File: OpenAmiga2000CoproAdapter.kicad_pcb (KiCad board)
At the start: 2 copper layers, 188.6 x 114.2 mm, 74 parts, among them CN1 A2000_COPRO_SLOT, P1 CONN_2, P10 CONN_1, P11 CONN_1, P12 CONN_1, P13 CONN_1, P14 CONN_1, P15 CONN_1, P2 CONN_2, P3 CONN_2, P4 CONN_2, P5 CONN_1, P6 CONN_1, P7 CONN_1, P8 CONN_1, P9 CONN_1, P99 OSHW_LOGO, U1 68000D, U10 Spare, U11 74HCT00, U12 74HCT27, U13 74HCT74, U14 74F86, U15 74F74, U16 74HCT04, U17 74HCT112, U18 74F157, U19 74F157, U2 AS6C4008-55PCN, U3 AS6C4008-55PCN, U4 AS6C4008-55PCN, U5 AS6C4008-55PCN, U6 74HCT00, U7 74HCT32, U8 74HCT32, U9 74LS05

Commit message: fix connector
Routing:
- net /~vpa: track 135.8 -> 135.2 mm
- net /e: track 105.2 -> 104.6 mm
- net /r_~w: track 191.0 -> 190.4 mm

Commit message: update silk screen
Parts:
- JP1: value 256K_512K -> 256K 512K
- JP10: value Turbo_SRAM -> Turbo SRAM
- JP2: value 1MB_512K -> 1MB xxxKB
- JP3: value Bank2 -> Bank 2
- JP4: value ROM_R_W -> ROM SW
- JP5: value Bank1_ON_OFF -> Bank 1
- JP6: value Mirror_OFF_ON -> Mirror 256K
- JP7: value Turbo -> Turbo SW
- JP8: value Bank2 D0_C0 -> Bank 2
- JP9: value Turbo_ROM -> Turbo ROM
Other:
- board text added: "C0 D0"
- board text added: "ON OFF"
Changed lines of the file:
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@@
   (general
     (thickness 1.6)
-    (drawings 121)
+    (drawings 124)
     (tracks 2299)
     (zones 0)
@@
     (descr "Through hole straight pin header, 1x03, 2.54mm pitch, single row")
     (tags "Through hole pin header THT 1x03 2.54mm single row")
-    (fp_text reference JP7 (at 0 -2.33) (layer F.SilkS)
+    (fp_text reference JP7 (at 0 7.62) (layer F.SilkS)
       (effects (font (size 1 1) (thickness 0.15)))
     )
-    (fp_text value Turbo (at 0 7.41) (layer F.Fab)
+    (fp_text value "Turbo SW" (at 2.54 2.54 90) (layer F.SilkS)
       (effects (font (size 1 1) (thickness 0.15)))
     )
@@
     (descr "14-lead though-hole mounted DIP package, row spacing 7.62 mm (300 mils)")
     (tags "THT DIP DIL PDIP 2.54mm 7.62mm 300mil")
-    (fp_text reference U16 (at 3.81 -2.33) (layer F.SilkS)
+    (fp_text reference U16 (at 3.81 18.415) (layer F.SilkS)
       (effects (font (size 1 1) (thickness 0.15)))
     )
-    (fp_text value 74HCT04 (at 3.81 17.57) (layer F.Fab)
+    (fp_text value 74HCT04 (at 3.81 7.62 90) (layer F.SilkS)
       (effects (font (size 1 1) (thickness 0.15)))
     )
@@
       (effects (font (size 1 1) (thickness 0.15)))
     )
-    (fp_text value 74HCT00 (at 3.81 17.57) (layer F.Fab)
+    (fp_text value 74HCT00 (at 3.81 7.62 90) (layer F.SilkS)
       (effects (font (size 1 1) (thickness 0.15)))
     )
@@
       (effects (font (size 1 1) (thickness 0.15)))
     )
-    (fp_text value "Bank2 D0_C0" (at 0 7.41) (layer F.Fab)
+    (fp_text value "Bank 2" (at -1.905 2.54 90) (layer F.SilkS)
       (effects (font (size 1 1) (thickness 0.15)))
     )
@@
     (descr "Through hole straight pin header, 1x03, 2.54mm pitch, single row")
     (tags "Through hole pin header THT 1x03 2.54mm single row")
-    (fp_text reference JP6 (at 0 -2.33) (layer F.SilkS)
+    (fp_text reference JP6 (at 0 7.62) (layer F.SilkS)
       (effects (font (size 1 1) (thickness 0.15)))
     )
-    (fp_text value Mirror_OFF_ON (at 0 7.41) (layer F.Fab)
+    (fp_text value "Mirror 256K" (at -1.905 2.54 90) (layer F.SilkS)
       (effects (font (size 1 1) (thickness 0.15)))
     )
@@
     (descr "Through hole straight pin header, 1x03, 2.54mm pitch, single row")
     (tags "Through hole pin header THT 1x03 2.54mm single row")
-    (fp_text reference JP4 (at 0 -2.33) (layer F.SilkS)
+    (fp_text reference JP4 (at 0 7.62) (layer F.SilkS)
       (effects (font (size 1 1) (thickness 0.15)))
     )
-    (fp_text value ROM_R_W (at 0 7.41) (layer F.Fab)
+    (fp_text value "ROM SW" (at 2.54 2.54 90) (layer F.SilkS)
       (effects (font (size 1 1) (thickness 0.15)))
     )
@@
     (descr "Through hole straight pin header, 1x02, 2.54mm pitch, single row")
     (tags "Through hole pin header THT 1x02 2.54mm single row")
-    (fp_text reference JP3 (at 0 -2.33) (layer F.SilkS)
+    (fp_text reference JP3 (at 0 5.08) (layer F.SilkS)
       (effects (font (size 1 1) (thickness 0.15)))
     )
-    (fp_text value Bank2 (at 0 4.87) (layer F.Fab)
+    (fp_text value "Bank 2" (at 2.54 1.27 90) (layer F.SilkS)
       (effects (font (size 1 1) (thickness 0.15)))
     )
@@
     (descr "Resistor, Axial_DIN0411 series, Axial, Horizontal, pin pitch=12.7mm, 1W, length*diameter=9.9*3.6mm^2")
     (tags "Resistor Axial_DIN0411 series Axial Horizontal pin pitch 12.7mm 1W length 9.9mm diameter 3.6mm")
-    (fp_text reference R3 (at 6.985 -7.62 90) (layer F.SilkS)
+    (fp_text reference R3 (at -2.54 0 180) (layer F.SilkS)
       (effects (font (size 1 1) (thickness 0.15)))
     )
@@
     (descr "Resistor, Axial_DIN0411 series, Axial, Horizontal, pin pitch=12.7mm, 1W, length*diameter=9.9*3.6mm^2")
     (tags "Resistor Axial_DIN0411 series Axial Horizontal pin pitch 12.7mm 1W length 9.9mm diameter 3.6mm")
-    (fp_text reference R1 (at -2.54 0 90) (layer F.SilkS)
+    (fp_text reference R1 (at -2.54 0 180) (layer F.SilkS)
       (effects (font (size 1 1) (thickness 0.15)))
     )
@@
     (descr "Through hole straight pin header, 1x02, 2.54mm pitch, single row")
     (tags "Through hole pin header THT 1x02 2.54mm single row")
-    (fp_text reference JP10 (at 0 -2.33) (layer F.SilkS)
+    (fp_text reference JP10 (at 0 5.08) (layer F.SilkS)
       (effects (font (size 1 1) (thickness 0.15)))
     )
-    (fp_text value Turbo_SRAM (at 2.54 1.27 90) (layer F.SilkS)
+    (fp_text value "Turbo SRAM" (at 2.54 1.27 90) (layer F.SilkS)
       (effects (font (size 1 1) (thickness 0.15)))
     )
@@
     (descr "Through hole straight pin header, 1x02, 2.54mm pitch, single row")
     (tags "Through hole pin header THT 1x02 2.54mm single row")
-    (fp_text reference JP9 (at 0 -2.33) (layer F.SilkS)
+    (fp_text reference JP9 (at 0 5.08) (layer F.SilkS)
       (effects (font (size 1 1) (thickness 0.15)))
     )
-    (fp_text value Turbo_ROM (at -2.54 1.27 90) (layer F.SilkS)
+    (fp_text value "Turbo ROM" (at 2.54 1.27 90) (layer F.SilkS)
       (effects (font (size 1 1) (thickness 0.15)))
     )
@@
       (effects (font (size 1 1) (thickness 0.15)))
     )
-    (fp_text value Bank1_ON_OFF (at 2.54 1.905 90) (layer F.SilkS)
+    (fp_text value "Bank 1" (at 2.54 2.54 90) (layer F.SilkS)
       (effects (font (size 1 1) (thickness 0.15)))
     )
@@
     (descr "Through hole straight pin header, 1x03, 2.54mm pitch, single row")
     (tags "Through hole pin header THT 1x03 2.54mm single row")
-    (fp_text reference JP2 (at 0 -2.33) (layer F.SilkS)
+    (fp_text reference JP2 (at 0 7.62) (layer F.SilkS)
       (effects (font (size 1 1) (thickness 0.15)))
     )
-    (fp_text value 1MB_512K (at 2.54 2.54 90) (layer F.SilkS)
+    (fp_text value "1MB xxxKB" (at -2.54 2.54 90) (layer F.SilkS)
       (effects (font (size 1 1) (thickness 0.15)))
     )
@@
     (descr "Through hole straight pin header, 1x03, 2.54mm pitch, single row")
     (tags "Through hole pin header THT 1x03 2.54mm single row")
-    (fp_text reference JP1 (at 0 -2.33) (layer F.SilkS)
+    (fp_text reference JP1 (at 0 7.62) (layer F.SilkS)
       (effects (font (size 1 1) (thickness 0.15)))
     )
-    (fp_text value 256K_512K (at -2.54 2.54 90) (layer F.SilkS)
+    (fp_text value "256K 512K" (at -1.905 2.54 90) (layer F.SilkS)
       (effects (font (size 1 1) (thickness 0.15)))
     )
@@
       (effects (font (size 1 1) (thickness 0.15)))
     )
-    (fp_text value 1N4001 (at 3.81 2.47 90) (layer F.Fab)
+    (fp_text value 1N4001 (at 3.81 2.47 90) (layer F.SilkS)
       (effects (font (size 1 1) (thickness 0.15)))
     )
@@
       (effects (font (size 1 1) (thickness 0.15)))
     )
-    (fp_text value 1N4001 (at 3.81 2.47 90) (layer F.Fab)
+    (fp_text value 1N4001 (at 3.81 2.47 90) (layer F.SilkS)
       (effects (font (size 1 1) (thickness 0.15)))
     )
@@
       (effects (font (size 1 1) (thickness 0.15)))
     )
-    (fp_text value 1N4001 (at 3.81 2.47) (layer F.Fab)
+    (fp_text value 1N4001 (at 3.81 2.47) (layer F.SilkS)
       (effects (font (size 1 1) (thickness 0.15)))
     )
@@
     (descr "C, Disc series, Radial, pin pitch=5.00mm, , diameter*width=7*2.5mm^2, Capacitor, http://cdn-reichelt.de/documents/datenblatt/B300/DS_KERKO_TC.pdf")
     (tags "C Disc series Radial pin pitch 5.00mm  diameter 7mm width 2.5mm Capacitor")
-    (fp_text reference C12 (at -3.89 0) (layer F.SilkS)
+    (fp_text reference C12 (at 2.46 2.54) (layer F.SilkS)
       (effects (font (size 1 1) (thickness 0.15)))
     )
@@
       (net 111 +12V))
   )
+  (gr_text "ON   OFF" (at 68.5165 74.93 90) (layer F.SilkS)
+    (effects (font (size 1 1) (thickness 0.15)))
+  )
+  (gr_text "ON   OFF" (at 69.7865 129.54 90) (layer F.SilkS)
+    (effects (font (size 1 1) (thickness 0.15)))
+  )
+  (gr_text "C0   D0" (at 69.1515 104.775 90) (layer F.SilkS)
+    (effects (font (size 1 1) (thickness 0.15)))
+  )
   (gr_text "Based on work by Kipper2K, SukkoPera, Livio Plos and Jörg Richter" (at 46.2915 87.63 90) (layer F.SilkS)
     (effects (font (size 1 1) (thickness 0.15)))
@@
   (via (at 65.9765 59.055) (size 0.8) (drill 0.5) (layers F.Cu B.Cu) (net 1))
   (via (at 67.2465 64.77) (size 0.8) (drill 0.5) (layers F.Cu B.Cu) (net 1))
-  (via (at 60.8965 80.01) (size 0.8) (drill 0.5) (layers F.Cu B.Cu) (net 1))
+  (via (at 60.8965 81.28) (size 0.8) (drill 0.5) (layers F.Cu B.Cu) (net 1))
   (segment (start 60.8965 84.455) (end 69.1515 84.455) (width 0.8) (layer B.Cu) (net 1))
   (via (at 60.8965 84.455) (size 0.8) (drill 0.5) (layers F.Cu B.Cu) (net 1))
@@
   (segment (start 153.11013 59.69) (end 151.84013 60.96) (width 0.25) (layer F.Cu) (net 116))
   (segment (start 154.2415 59.69) (end 153.11013 59.69) (width 0.25) (layer F.Cu) (net 116))
-  (segment (start 73.014002 76.055001) (end 67.736501 76.055001) (width 0.25) (layer B.Cu) (net 116))
-  (segment (start 73.5965 76.637499) (end 73.014002 76.055001) (width 0.25) (layer B.Cu) (net 116))
+  (segment (start 73.159001 76.2) (end 67.8815 76.2) (width 0.25) (layer B.Cu) (net 116))
+  (segment (start 67.8815 76.2) (end 66.6115 74.93) (width 0.25) (layer B.Cu) (net 116))
+  (segment (start 73.5965 76.637499) (end 73.159001 76.2) (width 0.25) (layer B.Cu) (net 116))
   (segment (start 73.5965 80.645) (end 73.5965 76.637499) (width 0.25) (layer B.Cu) (net 116))
-  (segment (start 87.5665 94.615) (end 73.5965 80.645) (width 0.25) (layer B.Cu) (net 116))
   (segment (start 88.8365 94.615) (end 87.5665 94.615) (width 0.25) (layer B.Cu) (net 116))
+  (segment (start 87.5665 94.615) (end 73.5965 80.645) (width 0.25) (layer B.Cu) (net 116))
   (segment (start 95.8215 87.63) (end 88.8365 94.615) (width 0.25) (layer B.Cu) (net 116))
   (segment (start 95.8215 67.31) (end 95.8215 87.63) (width 0.25) (layer B.Cu) (net 116))
-  (segment (start 67.736501 76.055001) (end 66.6115 74.93) (width 0.25) (layer B.Cu) (net 116))
   (segment (start 103.4415 59.69) (end 95.8215 67.31) (width 0.25) (layer B.Cu) (net 116))
   (segment (start 183.4515 63.5) (end 183.4515 71.12) (width 0.25) (layer F.Cu) (net 117))

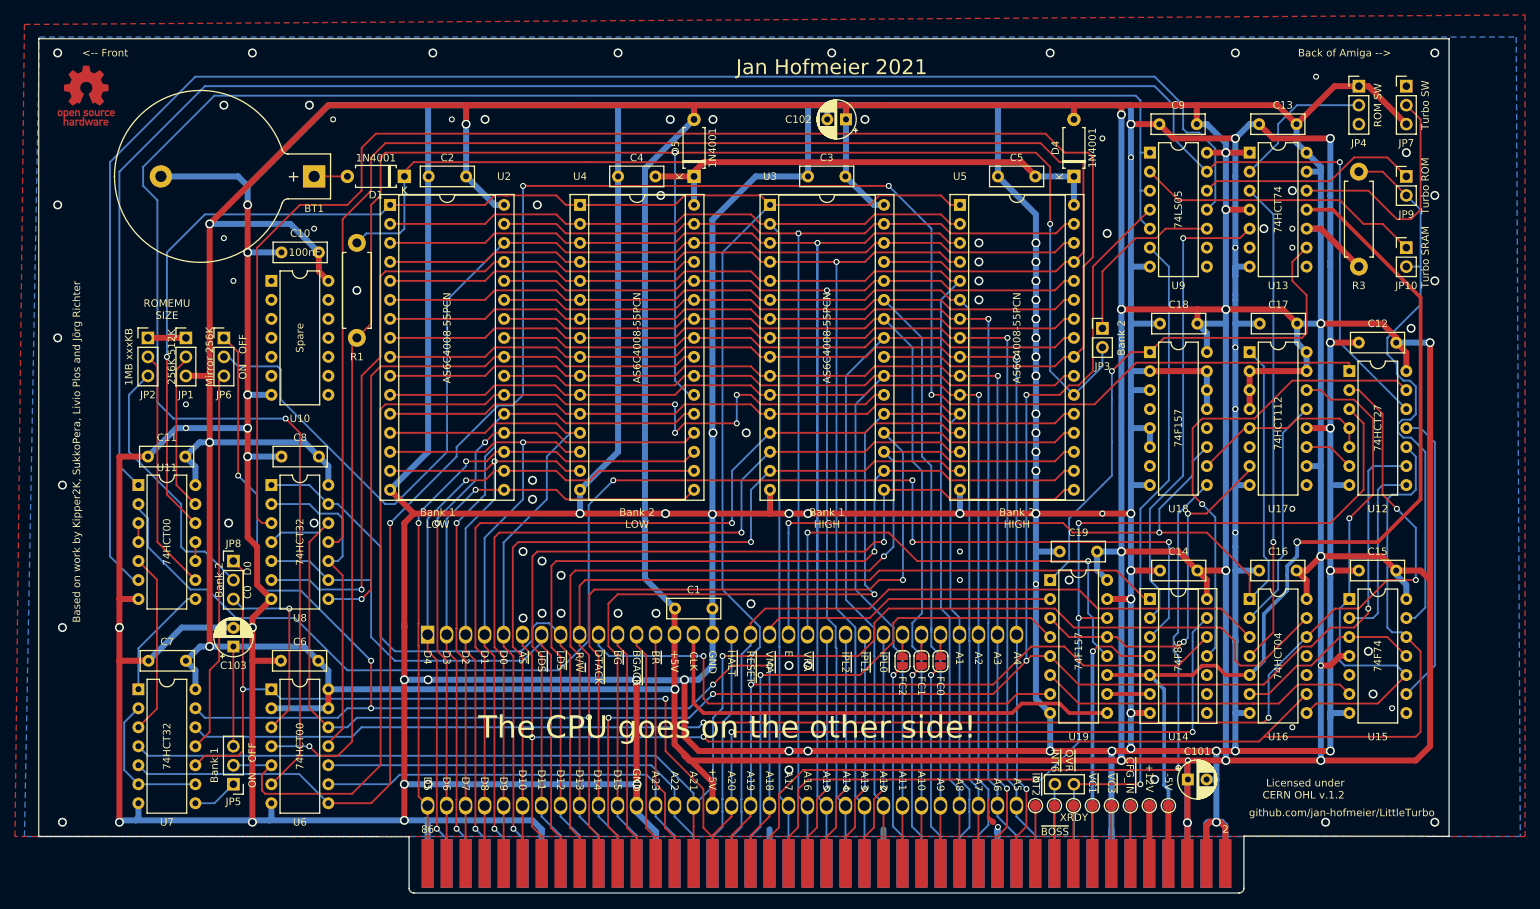
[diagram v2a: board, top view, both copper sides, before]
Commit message: shrink board
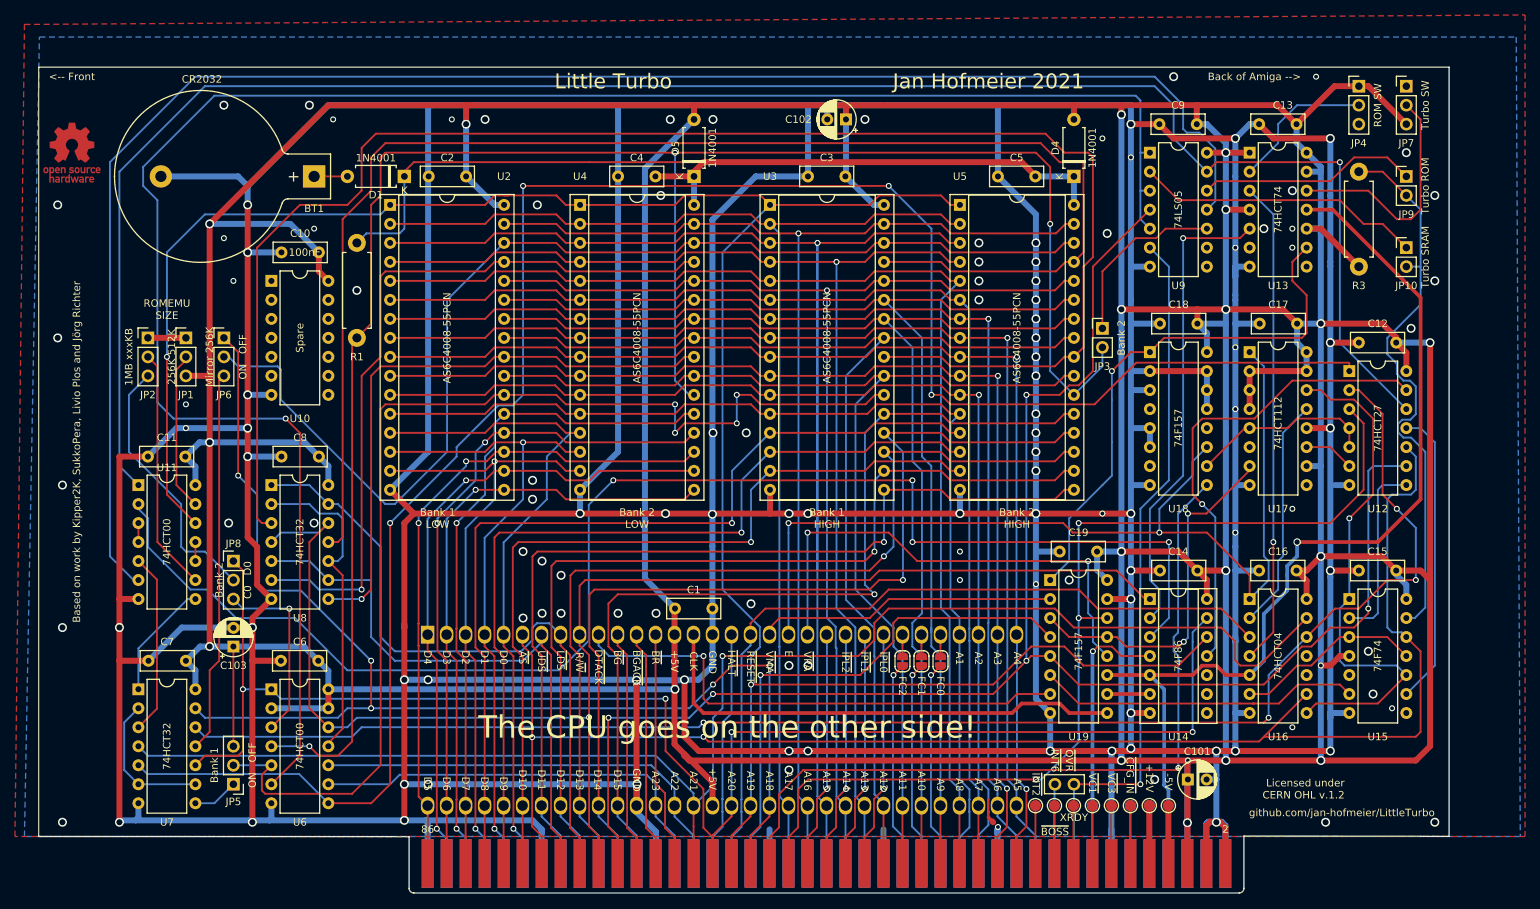
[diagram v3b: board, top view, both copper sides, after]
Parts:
- BT1: value Battery_Cell -> CR2032
- moved P99 7.85 mm to (45.7, 47.6)
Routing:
- net GND: vias 135 -> 128
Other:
- board size 188.6 x 114.2 mm -> 188.6 x 110.4 mm
- board text added: "Little Turbo"
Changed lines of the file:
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@@
     (thickness 1.6)
     (drawings 124)
-    (tracks 2299)
+    (tracks 2292)
     (zones 0)
     (modules 74)
@@
       (effects (font (size 1 1) (thickness 0.15)))
     )
-    (fp_text value Battery_Cell (at 15 13) (layer F.Fab)
+    (fp_text value CR2032 (at 15 13) (layer F.SilkS)
       (effects (font (size 1 1) (thickness 0.15)))
     )
@@
   )
   (module Symbol:OSHW-Logo_7.5x8mm_Copper (layer F.Cu)
-    (at 47.5615 40.005)
+    (at 45.6565 47.625)
     (descr "Open Source Hardware Logo")
     (tags "Logo OSHW")
@@
       (net 111 +12V))
   )
+  (gr_text "Little Turbo" (at 118.0465 38.1) (layer F.SilkS)
+    (effects (font (size 2 2) (thickness 0.15)))
+  )
   (gr_text "ON   OFF" (at 68.5165 74.93 90) (layer F.SilkS)
     (effects (font (size 1 1) (thickness 0.15)))
@@
     (effects (font (size 1 1) (thickness 0.15)))
   )
-  (gr_text "Jan Hofmeier 2021" (at 147.2565 36.195) (layer F.SilkS)
+  (gr_text "Jan Hofmeier 2021" (at 168.2115 38.1) (layer F.SilkS)
     (effects (font (size 2 2) (thickness 0.15)))
   )
-  (gr_text "Front -->" (at 50.1015 34.29) (layer B.SilkS)
+  (gr_text "Front -->" (at 45.6565 37.465) (layer B.SilkS)
     (effects (font (size 1 1) (thickness 0.15)) (justify mirror))
   )
-  (gr_text "<-- Front" (at 50.1015 34.29) (layer F.SilkS)
+  (gr_text "<-- Front" (at 45.6565 37.465) (layer F.SilkS)
     (effects (font (size 1 1) (thickness 0.15)))
   )
-  (gr_text "<-- Back of Amiga" (at 215.8365 34.29) (layer B.SilkS)
+  (gr_text "<-- Back of Amiga" (at 203.7715 37.465) (layer B.SilkS)
     (effects (font (size 1 1) (thickness 0.15)) (justify mirror))
   )
-  (gr_text "Back of Amiga -->" (at 215.8365 34.29) (layer F.SilkS)
+  (gr_text "Back of Amiga -->" (at 203.7715 37.465) (layer F.SilkS)
     (effects (font (size 1 1) (thickness 0.15)))
   )
@@
     (effects (font (size 3 3) (thickness 0.3)))
   )
-  (dimension 114.3 (width 0.05) (layer F.CrtYd)
-    (gr_text "114.300 mm" (at 30.4865 89.535 90) (layer F.CrtYd)
+  (dimension 110.49 (width 0.05) (layer F.CrtYd)
+    (gr_text "110.490 mm" (at 29.8515 91.44 90) (layer F.CrtYd)
       (effects (font (size 1 1) (thickness 0.15)))
     )
-    (feature1 (pts (xy 90.7415 32.385) (xy 31.100079 32.385)))
-    (feature2 (pts (xy 90.7415 146.685) (xy 31.100079 146.685)))
-    (crossbar (pts (xy 31.6865 146.685) (xy 31.6865 32.385)))
-    (arrow1a (pts (xy 31.6865 32.385) (xy 32.272921 33.511504)))
-    (arrow1b (pts (xy 31.6865 32.385) (xy 31.100079 33.511504)))
-    (arrow2a (pts (xy 31.6865 146.685) (xy 32.272921 145.558496)))
-    (arrow2b (pts (xy 31.6865 146.685) (xy 31.100079 145.558496)))
+    (feature1 (pts (xy 90.7415 36.195) (xy 30.465079 36.195)))
+    (feature2 (pts (xy 90.7415 146.685) (xy 30.465079 146.685)))
+    (crossbar (pts (xy 31.0515 146.685) (xy 31.0515 36.195)))
+    (arrow1a (pts (xy 31.0515 36.195) (xy 31.637921 37.321504)))
+    (arrow1b (pts (xy 31.0515 36.195) (xy 30.465079 37.321504)))
+    (arrow2a (pts (xy 31.0515 146.685) (xy 31.637921 145.558496)))
+    (arrow2b (pts (xy 31.0515 146.685) (xy 30.465079 145.558496)))
   )
   (dimension 188.595 (width 0.05) (layer F.CrtYd)
@@
     (effects (font (size 1 1) (thickness 0.2)))
   )
-  (gr_line (start 41.2115 32.385) (end 41.2115 33.02) (layer Edge.Cuts) (width 0.15))
-  (gr_line (start 229.8065 32.385) (end 41.2115 32.385) (layer Edge.Cuts) (width 0.15))
-  (gr_line (start 229.8065 139.0523) (end 229.8065 32.385) (layer Edge.Cuts) (width 0.15))
+  (gr_line (start 229.8065 36.195) (end 41.2115 36.195) (layer Edge.Cuts) (width 0.15))
+  (gr_line (start 229.8065 139.0523) (end 229.8065 36.195) (layer Edge.Cuts) (width 0.15))
   (gr_line (start 90.7415 139.0904) (end 41.2115 139.065) (layer Edge.Cuts) (width 0.15))
-  (gr_line (start 41.2115 139.065) (end 41.2115 33.02) (layer Edge.Cuts) (width 0.15))
-  (dimension 114.3 (width 0.05) (layer B.CrtYd)
-    (gr_text "114,300 mm" (at 20.517 81.915 90) (layer B.CrtYd)
+  (gr_line (start 41.2115 139.065) (end 41.2115 36.195) (layer Edge.Cuts) (width 0.15))
+  (dimension 102.87 (width 0.05) (layer B.CrtYd)
+    (gr_text "102.870 mm" (at 20.517 87.63 90) (layer B.CrtYd)
       (effects (font (size 1 1) (thickness 0.15)))
     )
-    (feature1 (pts (xy 29.845 24.765) (xy 21.130579 24.765)))
+    (feature1 (pts (xy 29.845 36.195) (xy 21.130579 36.195)))
     (feature2 (pts (xy 29.845 139.065) (xy 21.130579 139.065)))
-    (crossbar (pts (xy 21.717 139.065) (xy 21.717 24.765)))
-    (arrow1a (pts (xy 21.717 24.765) (xy 22.303421 25.891504)))
-    (arrow1b (pts (xy 21.717 24.765) (xy 21.130579 25.891504)))
+    (crossbar (pts (xy 21.717 139.065) (xy 21.717 36.195)))
+    (arrow1a (pts (xy 21.717 36.195) (xy 22.303421 37.321504)))
+    (arrow1b (pts (xy 21.717 36.195) (xy 21.130579 37.321504)))
     (arrow2a (pts (xy 21.717 139.065) (xy 22.303421 137.938496)))
     (arrow2b (pts (xy 21.717 139.065) (xy 21.130579 137.938496)))
@@
   (via (at 213.9315 45.72) (size 1.2) (drill 0.8) (layers F.Cu B.Cu) (net 1))
   (via (at 44.3865 137.16) (size 1.2) (drill 0.8) (layers F.Cu B.Cu) (net 1))
-  (via (at 43.7515 34.29) (size 1.2) (drill 0.8) (layers F.Cu B.Cu) (net 1))
   (via (at 44.3865 111.125) (size 1.2) (drill 0.8) (layers F.Cu B.Cu) (net 1))
   (via (at 44.3865 92.075) (size 1.2) (drill 0.8) (layers F.Cu B.Cu) (net 1))
   (via (at 208.8515 52.705) (size 1.2) (drill 0.8) (layers F.Cu B.Cu) (net 1))
   (via (at 205.0415 57.785) (size 1.2) (drill 0.8) (layers F.Cu B.Cu) (net 1))
-  (via (at 227.9015 34.29) (size 1.2) (drill 0.8) (layers F.Cu B.Cu) (net 1))
   (via (at 227.9015 53.34) (size 1.2) (drill 0.8) (layers F.Cu B.Cu) (net 1))
-  (via (at 201.2315 34.29) (size 1.2) (drill 0.8) (layers F.Cu B.Cu) (net 1))
-  (via (at 176.4665 34.29) (size 1.2) (drill 0.8) (layers F.Cu B.Cu) (net 1))
-  (via (at 147.2565 34.29) (size 1.2) (drill 0.8) (layers F.Cu B.Cu) (net 1))
-  (via (at 118.6815 34.29) (size 1.2) (drill 0.8) (layers F.Cu B.Cu) (net 1))
-  (via (at 93.9165 34.29) (size 1.2) (drill 0.8) (layers F.Cu B.Cu) (net 1))
-  (via (at 69.7865 34.29) (size 1.2) (drill 0.8) (layers F.Cu B.Cu) (net 1))
+  (via (at 192.9765 37.465) (size 1.2) (drill 0.8) (layers F.Cu B.Cu) (net 1))
   (via (at 135.8265 85.09) (size 1.2) (drill 0.8) (layers F.Cu B.Cu) (net 1))
   (via (at 131.3815 85.09) (size 1.2) (drill 0.8) (layers F.Cu B.Cu) (net 1))
